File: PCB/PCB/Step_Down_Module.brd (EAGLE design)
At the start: 160 x 100 mm, 4 parts, among them Q1 TPH2900ENH

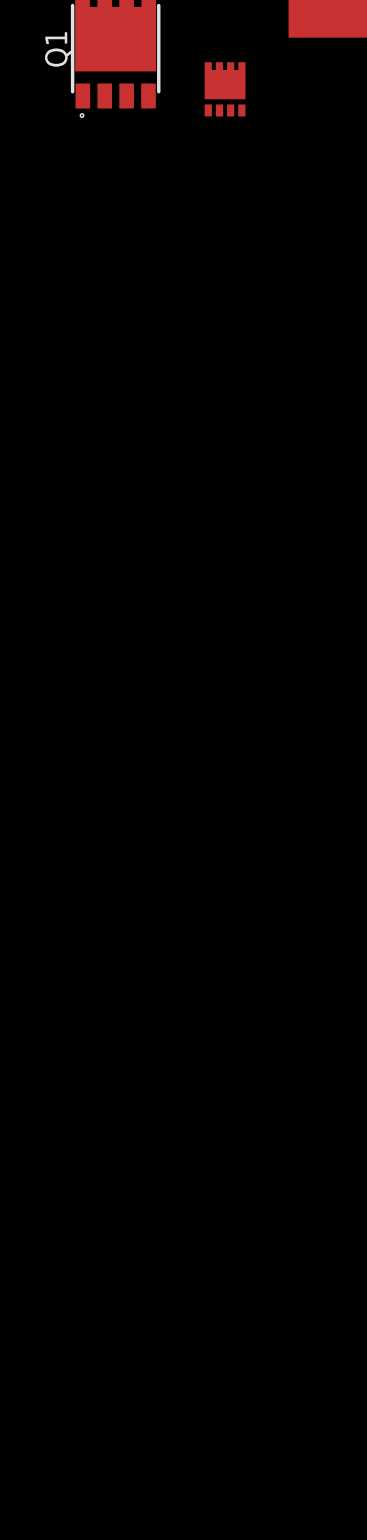
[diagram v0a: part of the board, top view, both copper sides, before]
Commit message: Working on schematic, slightly updated mosfets
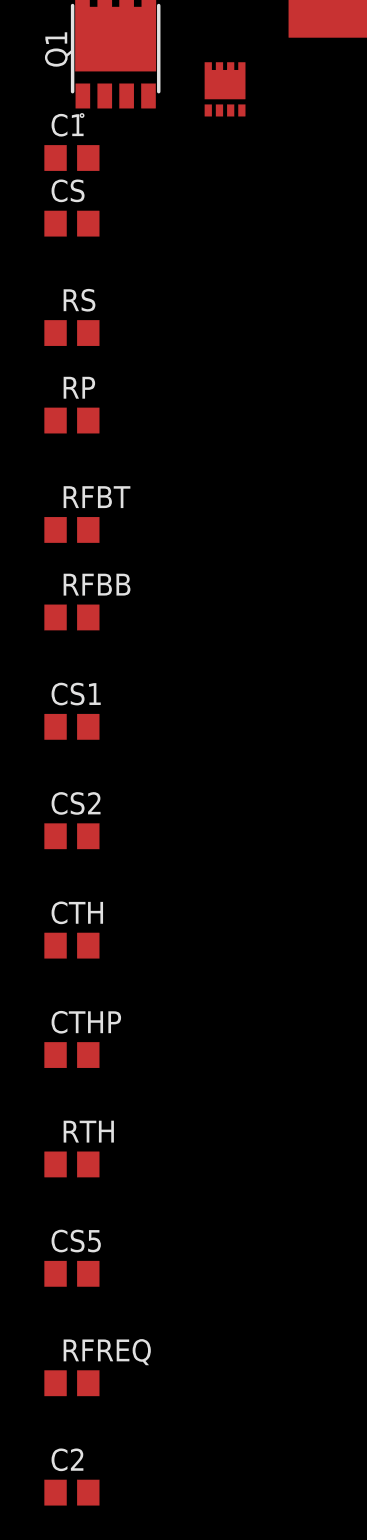
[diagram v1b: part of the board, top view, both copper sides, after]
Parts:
- added C1, C2: 0.1uF, rcl:C0805
- added CS, CS1, CS2, CS5: 0.01uF, rcl:C0805
- added CTH: 4700pf, rcl:C0805
- added CTHP: 100pf, rcl:C0805
- added RFBB, RTH: 10k, rcl:R0805
- added RFBT: 390k, rcl:R0805
- added RFREQ: 110k, rcl:R0805
- added RP: 10000k, rcl:R0805
- added RS: 280K, rcl:R0805
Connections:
- new net GND: C2.1, CS2.1, CS5.2, CTH.2, CTHP.2, Q1.S_1, Q1.S_2, Q1.S_3, RFBB.1, RFREQ.1
- new net N$1: U$1.20, U$3.G
- new net N$10: CTHP.1, RTH.1, U$1.7
- new net N$11: RFREQ.2, U$1.17
- new net N$12: CTH.1, RTH.2
- new net N$13: C2.2, U$1.10, U$1.38
- new net N$2: Q1.G, U$1.24
- new net N$3: C1.2, Q1.D, Q1.D_1, Q1.D_2, Q1.D_3, Q1.D_4, RS.2, U$1.21, U$2.P2, U$3.S_1, U$3.S_2, U$3.S_3
- new net N$4: C1.1, U$1.22
- new net N$5: CS.1, CS1.2, RFBT.2, RP.1, U$1.4, U$2.P1
- new net N$6: CS.2, RP.2, RS.1, U$1.3
- new net N$7: CS5.1, U$1.5
- new net N$8: CS1.1, CS2.2, RFBB.2, RFBT.1, U$1.6
- new net N$9: U$1.30, U$1.34, U$3.D, U$3.D_1, U$3.D_2, U$3.D_3, U$3.D_4

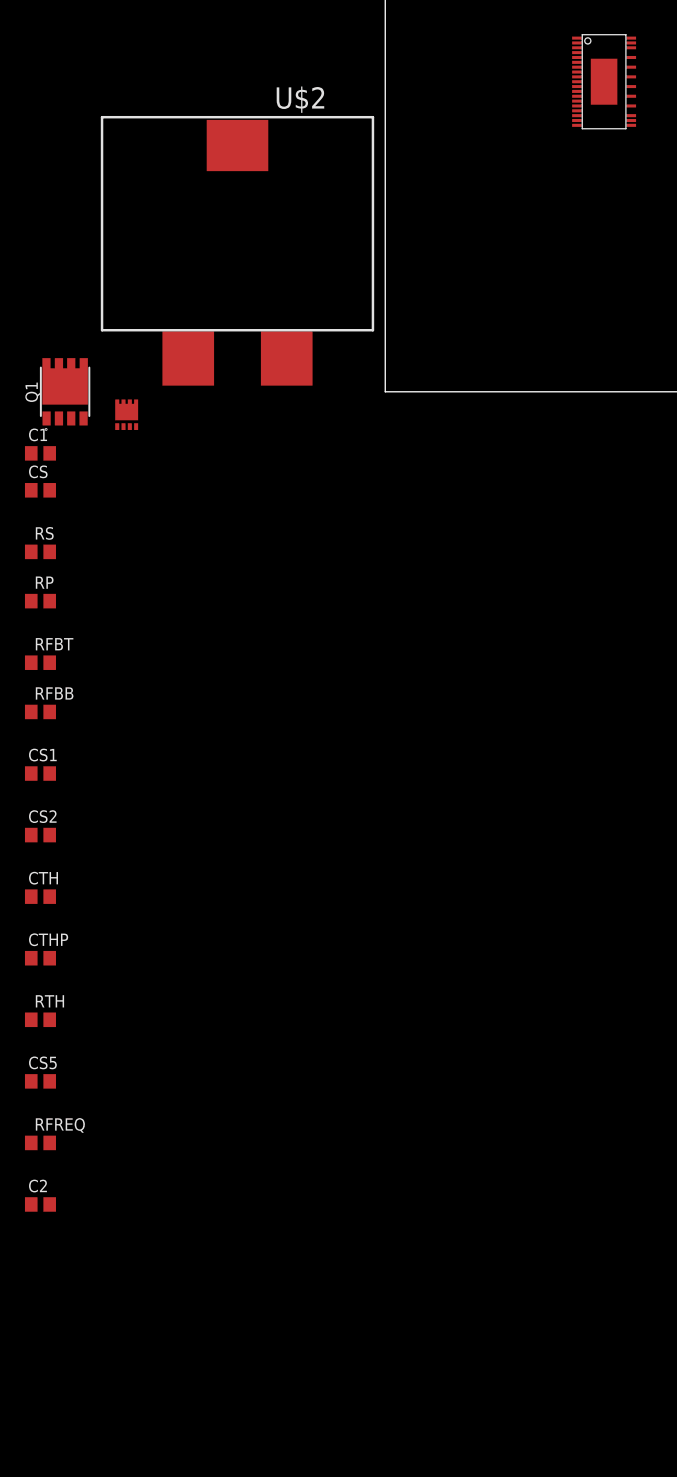
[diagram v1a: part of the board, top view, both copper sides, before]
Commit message: Working on schematic - functions of other pins
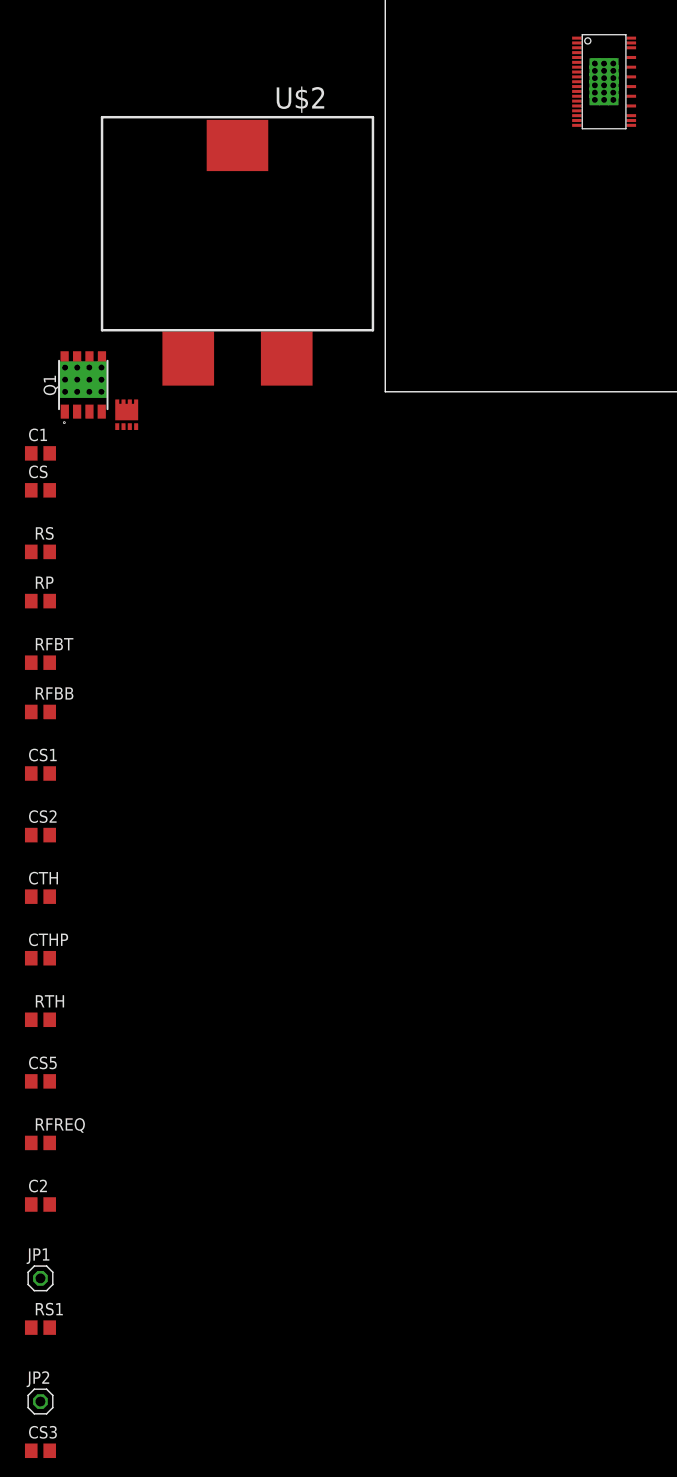
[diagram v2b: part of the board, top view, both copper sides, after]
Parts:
- added CS3: 4.7uF, rcl:C0805
- added JP1, JP2: (no value), pinhead:1X01
- added RS1: 100k, rcl:R0805
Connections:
- removed net N$13: C2.2, U$1.10, U$1.38
- new net CLKOUT: JP2.1, U$1.11
- new net INTVCC: C2.2, RS1.2, U$1.10, U$1.19, U$1.38
- new net N$14: CS3.1, U$1.26, U$1.28
- new net PGOOD: JP1.1, RS1.1, U$1.14
- net GND: now also CS3.2, U$1.1, U$1.12, U$1.15, U$1.36, U$1.39, U$1.8, U$1.9, U$1.PWR_PAD1, U$1.PWR_PAD10, U$1.PWR_PAD11, U$1.PWR_PAD12, U$1.PWR_PAD13, U$1.PWR_PAD14, U$1.PWR_PAD15, U$1.PWR_PAD16, U$1.PWR_PAD17, U$1.PWR_PAD18, U$1.PWR_PAD2, U$1.PWR_PAD3, U$1.PWR_PAD4, U$1.PWR_PAD5, U$1.PWR_PAD6, U$1.PWR_PAD7, U$1.PWR_PAD8, U$1.PWR_PAD9
- net N$3: now also Q1.PWR_PAD1, Q1.PWR_PAD10, Q1.PWR_PAD11, Q1.PWR_PAD12, Q1.PWR_PAD2, Q1.PWR_PAD3, Q1.PWR_PAD4, Q1.PWR_PAD5, Q1.PWR_PAD6, Q1.PWR_PAD7, Q1.PWR_PAD8, Q1.PWR_PAD9
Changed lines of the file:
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@@
 <attribute name="SPICEPREFIX" value="C" x="-35.56" y="-83.82" size="1.778" layer="27" display="off"/>
+</element>
+<element name="JP1" library="pinhead" library_urn="urn:adsk.eagle:library:325" package="1X01" package3d_urn="urn:adsk.eagle:package:22485/2" value="" x="-35.56" y="-91.44"/>
+<element name="RS1" library="rcl" library_urn="urn:adsk.eagle:library:334" package="R0805" package3d_urn="urn:adsk.eagle:package:23553/2" value="100k" x="-35.56" y="-96.52">
+<attribute name="SPICEPREFIX" value="R" x="-35.56" y="-96.52" size="1.778" layer="27" display="off"/>
+</element>
+<element name="JP2" library="pinhead" library_urn="urn:adsk.eagle:library:325" package="1X01" package3d_urn="urn:adsk.eagle:package:22485/2" value="" x="-35.56" y="-104.14"/>
+<element name="CS3" library="rcl" library_urn="urn:adsk.eagle:library:334" package="C0805" package3d_urn="urn:adsk.eagle:package:23617/2" value="4.7uF" x="-35.56" y="-109.22">
+<attribute name="SPICEPREFIX" value="C" x="-35.56" y="-109.22" size="1.778" layer="27" display="off"/>
 </element>
 </elements>
@@
 <contactref element="U$1" pad="24"/>
 <contactref element="Q1" pad="G"/>
-<wire x1="-31.115" y1="-2.75" x2="25.345" y2="29.48" width="0" layer="19" extent="1-1"/>
+<wire x1="-29.24" y1="-2.045" x2="25.345" y2="29.48" width="0" layer="19" extent="1-1"/>
 </signal>
 <signal name="N$3">
@@
 <wire x1="-26.995" y1="-3.59" x2="-26.345" y2="-3.59" width="0" layer="19" extent="1-1"/>
 <wire x1="-27.645" y1="-3.59" x2="-26.995" y2="-3.59" width="0" layer="19" extent="1-1"/>
-<wire x1="-33.02" y1="0.55" x2="-27.645" y2="-3.59" width="0" layer="19" extent="1-1"/>
-<wire x1="-33.655" y1="2.95" x2="-33.02" y2="0.55" width="0" layer="19" extent="1-1"/>
-<wire x1="-32.385" y1="2.95" x2="-33.655" y2="2.95" width="0" layer="19" extent="1-1"/>
-<wire x1="-34.945" y1="2.95" x2="-33.655" y2="2.95" width="0" layer="19" extent="1-1"/>
-<wire x1="-31.095" y1="2.95" x2="-32.385" y2="2.95" width="0" layer="19" extent="1-1"/>
-<wire x1="-34.61" y1="-6.35" x2="-33.02" y2="0.55" width="0" layer="19" extent="1-1"/>
+<wire x1="-31.145" y1="1.255" x2="-27.645" y2="-3.59" width="0" layer="19" extent="1-1"/>
+<wire x1="-31.78" y1="3.655" x2="-31.145" y2="1.255" width="0" layer="19" extent="1-1"/>
+<wire x1="-30.51" y1="3.655" x2="-31.78" y2="3.655" width="0" layer="19" extent="1-1"/>
+<wire x1="-33.07" y1="3.655" x2="-31.78" y2="3.655" width="0" layer="19" extent="1-1"/>
+<wire x1="-29.22" y1="3.655" x2="-30.51" y2="3.655" width="0" layer="19" extent="1-1"/>
+<wire x1="-34.61" y1="-6.35" x2="-31.145" y2="1.255" width="0" layer="19" extent="1-1"/>
 <wire x1="-34.61" y1="-16.51" x2="-34.61" y2="-6.35" width="0" layer="19" extent="1-1"/>
+<contactref element="Q1" pad="PWR_PAD1"/>
+<contactref element="Q1" pad="PWR_PAD2"/>
+<contactref element="Q1" pad="PWR_PAD3"/>
+<contactref element="Q1" pad="PWR_PAD4"/>
+<contactref element="Q1" pad="PWR_PAD5"/>
+<contactref element="Q1" pad="PWR_PAD6"/>
+<contactref element="Q1" pad="PWR_PAD7"/>
+<contactref element="Q1" pad="PWR_PAD8"/>
+<contactref element="Q1" pad="PWR_PAD9"/>
+<contactref element="Q1" pad="PWR_PAD10"/>
+<contactref element="Q1" pad="PWR_PAD11"/>
+<contactref element="Q1" pad="PWR_PAD12"/>
 </signal>
 <signal name="N$4">
@@
 <contactref element="RFREQ" pad="1"/>
 <contactref element="C2" pad="1"/>
+<contactref element="U$1" pad="1"/>
+<contactref element="U$1" pad="PWR_PAD18"/>
+<contactref element="U$1" pad="PWR_PAD2"/>
+<contactref element="U$1" pad="PWR_PAD9"/>
+<contactref element="U$1" pad="39"/>
+<contactref element="U$1" pad="PWR_PAD17"/>
+<contactref element="U$1" pad="9"/>
+<contactref element="U$1" pad="12"/>
+<contactref element="U$1" pad="PWR_PAD6"/>
+<contactref element="U$1" pad="PWR_PAD15"/>
+<contactref element="U$1" pad="PWR_PAD4"/>
+<contactref element="U$1" pad="PWR_PAD10"/>
+<contactref element="U$1" pad="PWR_PAD16"/>
+<contactref element="U$1" pad="PWR_PAD14"/>
+<contactref element="U$1" pad="PWR_PAD1"/>
+<contactref element="U$1" pad="15"/>
+<contactref element="U$1" pad="PWR_PAD8"/>
+<contactref element="U$1" pad="PWR_PAD7"/>
+<contactref element="U$1" pad="PWR_PAD5"/>
+<contactref element="U$1" pad="PWR_PAD3"/>
+<contactref element="U$1" pad="PWR_PAD12"/>
+<contactref element="U$1" pad="PWR_PAD11"/>
+<contactref element="U$1" pad="PWR_PAD13"/>
+<contactref element="U$1" pad="8"/>
+<contactref element="U$1" pad="36"/>
+<contactref element="CS3" pad="2"/>
+<wire x1="-36.51" y1="-83.82" x2="-34.61" y2="-109.22" width="0" layer="19" extent="1-1"/>
 <wire x1="-36.51" y1="-77.47" x2="-36.51" y2="-83.82" width="0" layer="19" extent="1-1"/>
 <wire x1="-34.61" y1="-71.12" x2="-36.51" y2="-77.47" width="0" layer="19" extent="1-1"/>
@@
 <wire x1="-36.51" y1="-45.72" x2="-34.61" y2="-52.07" width="0" layer="19" extent="1-1"/>
 <wire x1="-36.51" y1="-33.02" x2="-36.51" y2="-45.72" width="0" layer="19" extent="1-1"/>
-<wire x1="-34.925" y1="-2.75" x2="-36.51" y2="-33.02" width="0" layer="19" extent="1-1"/>
-<wire x1="-33.655" y1="-2.75" x2="-34.925" y2="-2.75" width="0" layer="19" extent="1-1"/>
-<wire x1="-32.385" y1="-2.75" x2="-33.655" y2="-2.75" width="0" layer="19" extent="1-1"/>
+<wire x1="-33.05" y1="-2.045" x2="-36.51" y2="-33.02" width="0" layer="19" extent="1-1"/>
+<wire x1="-31.78" y1="-2.045" x2="-33.05" y2="-2.045" width="0" layer="19" extent="1-1"/>
+<wire x1="-30.51" y1="-2.045" x2="-31.78" y2="-2.045" width="0" layer="19" extent="1-1"/>
+<wire x1="19.795" y1="29.48" x2="-30.51" y2="-2.045" width="0" layer="19" extent="1-1"/>
+<wire x1="19.795" y1="30.98" x2="19.795" y2="29.48" width="0" layer="19" extent="1-1"/>
+<wire x1="19.795" y1="32.48" x2="19.795" y2="30.98" width="0" layer="19" extent="1-1"/>
+<wire x1="19.795" y1="32.98" x2="19.795" y2="32.48" width="0" layer="19" extent="1-1"/>
+<wire x1="21.62" y1="33.105" x2="19.795" y2="32.98" width="0" layer="19" extent="1-1"/>
+<wire x1="21.62" y1="33.855" x2="21.62" y2="33.105" width="0" layer="19" extent="1-1"/>
+<wire x1="21.62" y1="32.355" x2="21.62" y2="33.105" width="0" layer="19" extent="1-1"/>
+<wire x1="21.62" y1="31.605" x2="21.62" y2="32.355" width="0" layer="19" extent="1-1"/>
+<wire x1="21.62" y1="30.855" x2="21.62" y2="31.605" width="0" layer="19" extent="1-1"/>
+<wire x1="21.62" y1="30.105" x2="21.62" y2="30.855" width="0" layer="19" extent="1-1"/>
+<wire x1="22.57" y1="33.855" x2="21.62" y2="33.855" width="0" layer="19" extent="1-1"/>
+<wire x1="22.57" y1="33.105" x2="22.57" y2="33.855" width="0" layer="19" extent="1-1"/>
+<wire x1="22.57" y1="32.355" x2="22.57" y2="33.105" width="0" layer="19" extent="1-1"/>
+<wire x1="22.57" y1="31.98" x2="22.57" y2="32.355" width="0" layer="19" extent="1-1"/>
+<wire x1="22.57" y1="31.605" x2="22.57" y2="31.98" width="0" layer="19" extent="1-1"/>
+<wire x1="22.57" y1="30.855" x2="22.57" y2="31.605" width="0" layer="19" extent="1-1"/>
+<wire x1="22.57" y1="30.105" x2="22.57" y2="30.855" width="0" layer="19" extent="1-1"/>
+<wire x1="23.52" y1="33.105" x2="22.57" y2="33.105" width="0" layer="19" extent="1-1"/>
+<wire x1="23.52" y1="33.855" x2="23.52" y2="33.105" width="0" layer="19" extent="1-1"/>
+<wire x1="23.52" y1="32.355" x2="23.52" y2="33.105" width="0" layer="19" extent="1-1"/>
+<wire x1="23.52" y1="31.605" x2="23.52" y2="32.355" width="0" layer="19" extent="1-1"/>
+<wire x1="23.52" y1="30.855" x2="23.52" y2="31.605" width="0" layer="19" extent="1-1"/>
+<wire x1="23.52" y1="30.105" x2="23.52" y2="30.855" width="0" layer="19" extent="1-1"/>
+<wire x1="25.345" y1="35.48" x2="23.52" y2="33.855" width="0" layer="19" extent="1-1"/>
+<wire x1="19.795" y1="36.48" x2="21.62" y2="33.855" width="0" layer="19" extent="1-1"/>
 </signal>
 <signal name="N$7">
@@
 <wire x1="19.795" y1="28.48" x2="-34.61" y2="-77.47" width="0" layer="19" extent="1-1"/>
 </signal>
-<signal name="N$13">
+<signal name="INTVCC">
 <contactref element="C2" pad="2"/>
 <contactref element="U$1" pad="38"/>
 <contactref element="U$1" pad="10"/>
-<wire x1="19.795" y1="31.98" x2="-34.61" y2="-83.82" width="0" layer="19" extent="1-1"/>
+<contactref element="RS1" pad="2"/>
+<contactref element="U$1" pad="19"/>
+<wire x1="-34.61" y1="-83.82" x2="-34.61" y2="-96.52" width="0" layer="19" extent="1-1"/>
+<wire x1="19.795" y1="27.48" x2="-34.61" y2="-83.82" width="0" layer="19" extent="1-1"/>
+<wire x1="19.795" y1="31.98" x2="19.795" y2="27.48" width="0" layer="19" extent="1-1"/>
 <wire x1="25.345" y1="36.48" x2="19.795" y2="31.98" width="0" layer="19" extent="1-1"/>
 </signal>
+<signal name="PGOOD">
+<contactref element="U$1" pad="14"/>
+<contactref element="JP1" pad="1"/>
+<contactref element="RS1" pad="1"/>
+<wire x1="-35.56" y1="-91.44" x2="-36.51" y2="-96.52" width="0" layer="19" extent="1-1"/>
+<wire x1="19.795" y1="29.98" x2="-35.56" y2="-91.44" width="0" layer="19" extent="1-1"/>
+</signal>
+<signal name="CLKOUT">
+<contactref element="U$1" pad="11"/>
+<contactref element="JP2" pad="1"/>
+<wire x1="19.795" y1="31.48" x2="-35.56" y2="-104.14" width="0" layer="19" extent="1-1"/>
+</signal>
+<signal name="N$14">
+<contactref element="U$1" pad="28"/>
+<contactref element="U$1" pad="26"/>
+<contactref element="CS3" pad="1"/>
+<wire x1="25.345" y1="30.48" x2="-36.51" y2="-109.22" width="0" layer="19" extent="1-1"/>
+<wire x1="25.345" y1="31.48" x2="25.345" y2="30.48" width="0" layer="19" extent="1-1"/>
+</signal>
 </signals>
